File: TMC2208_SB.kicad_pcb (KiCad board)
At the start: 4 copper layers, 15.2 x 20.3 mm, 26 parts, among them J1 Conn_01x08, J2 Conn_01x08, J3 Conn_01x01, J4 Conn_01x01, J5 Conn_01x01, P22 MOUNT 3.6mm, P23 MOUNT 3.6mm, U3 TMC2208

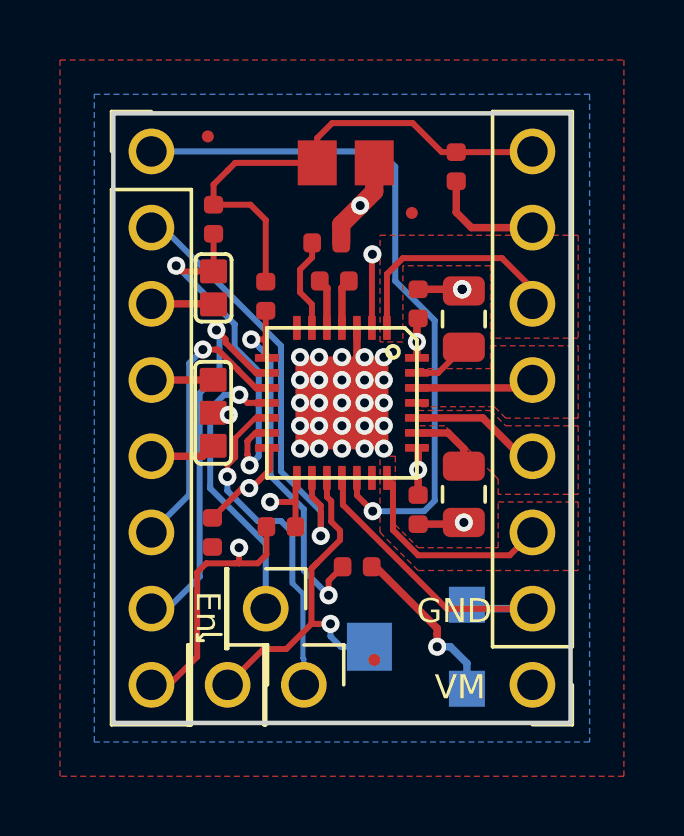
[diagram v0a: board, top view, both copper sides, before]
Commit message: silk revision, resistor clean up
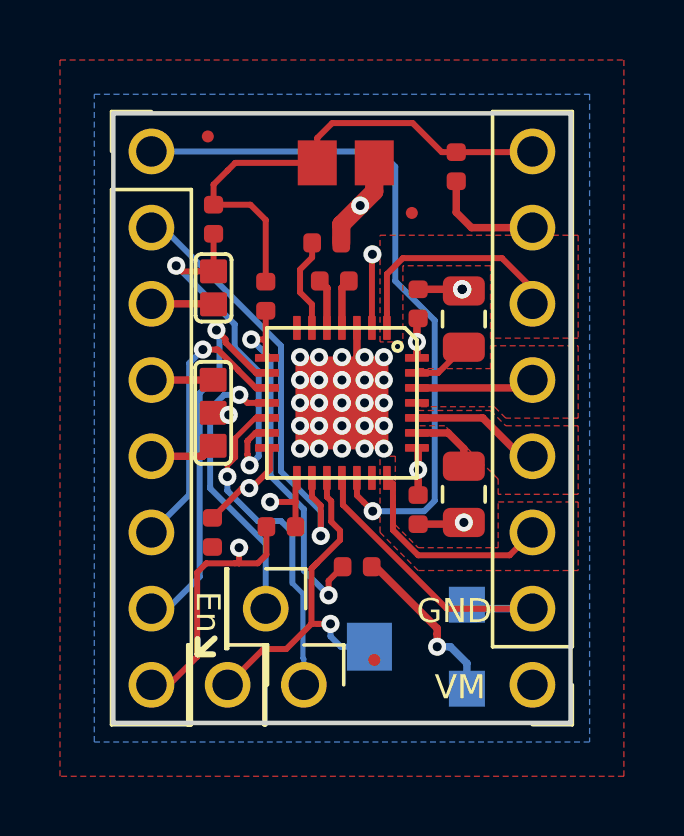
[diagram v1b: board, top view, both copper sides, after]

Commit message: lots of cosmetic changes
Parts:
- R1, R15, R2, R3: value 20K -> 10K
- moved P23 2.75 mm to (120.3, 110.8)
- moved C3 0.27 mm to (125.3, 114.2)
- moved C2 0.25 mm to (120.3, 113.9)
- moved C4 0.17 mm to (125.3, 121.5)
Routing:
- net GND: track 33.8 -> 35.8 mm, vias 28 -> 27
